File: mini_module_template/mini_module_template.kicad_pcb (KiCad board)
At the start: 4 copper layers, 100 x 50 mm, 135 parts, among them IC1 TJA1044GTK_3Z, J1 SWD, J4 USB_C_Receptacle_USB2.0, Q1 S9013, SW2 NRST, SW4 SW_DIP_x01, U1 STM32F303CBTx, U2 FM24CL16B, U3 STM32F103CB, U4 AZ1117-3.3, U5 TPS563200, U6 IP4220CZ6, U7 SL2.1A, Y1 8MHz, Y2 8MHz, Y4 12Mhz

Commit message: a
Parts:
- moved R35 0.42 mm to (165.2, 68.4)
- moved C33 0.39 mm to (165.4, 70.2)
- moved R33 0.16 mm to (164.0, 65.4)
- moved R34 0.16 mm to (164.0, 66.6)
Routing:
- net GND: track 95.7 -> 102.7 mm, vias 72 -> 76
- net /USB/USB_PROT_D+: track 6.66 -> 10.1 mm
- net +3V3: track 16.5 -> 19.4 mm, vias 32 -> 34
- net Net-(D1-A): track 25.4 -> 23.7 mm
- net /CAN/CANH: track 143.0 -> 144.6 mm
- net /MCU/USB_D-: track 41.1 -> 41.7 mm

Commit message: a
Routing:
- net /CAN/CANH: track 144.6 -> 109.2 mm
- net /CAN/CANL: track 146.0 -> 115.4 mm

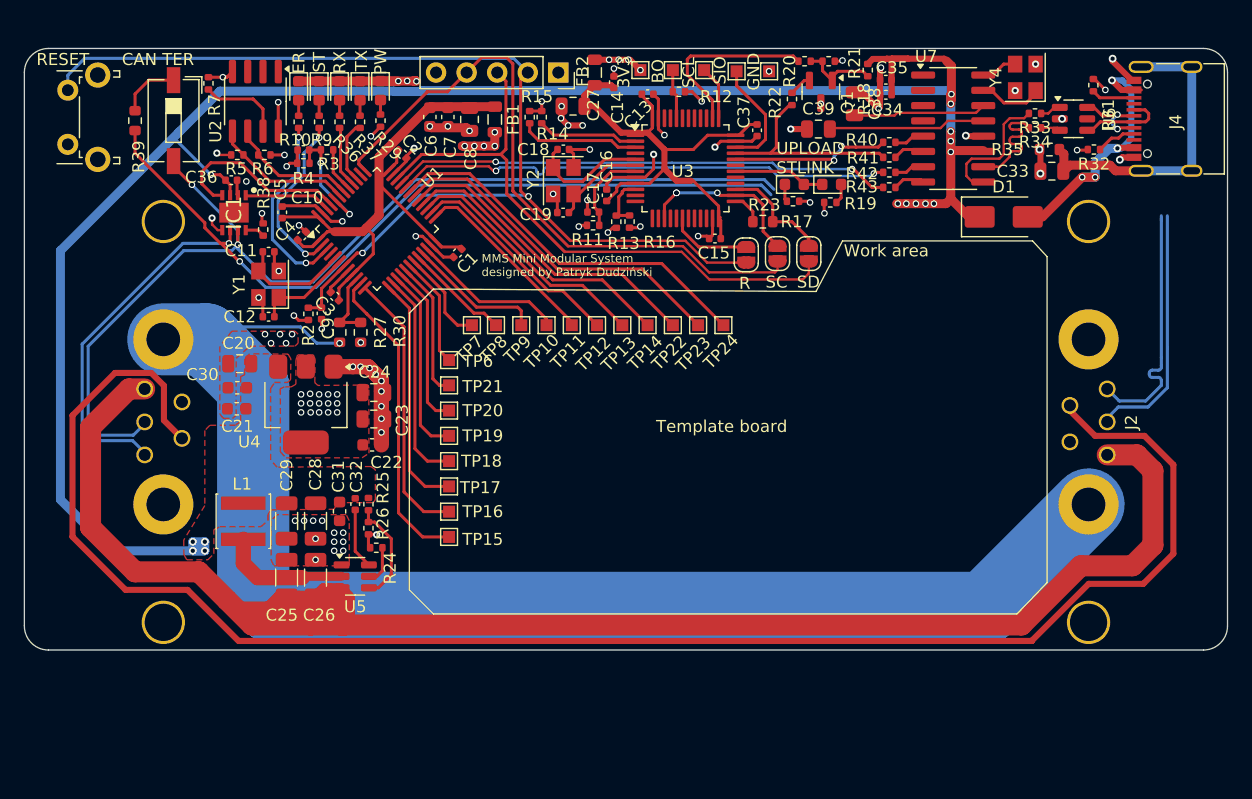
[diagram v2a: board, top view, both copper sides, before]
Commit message: fixed can and usb traces
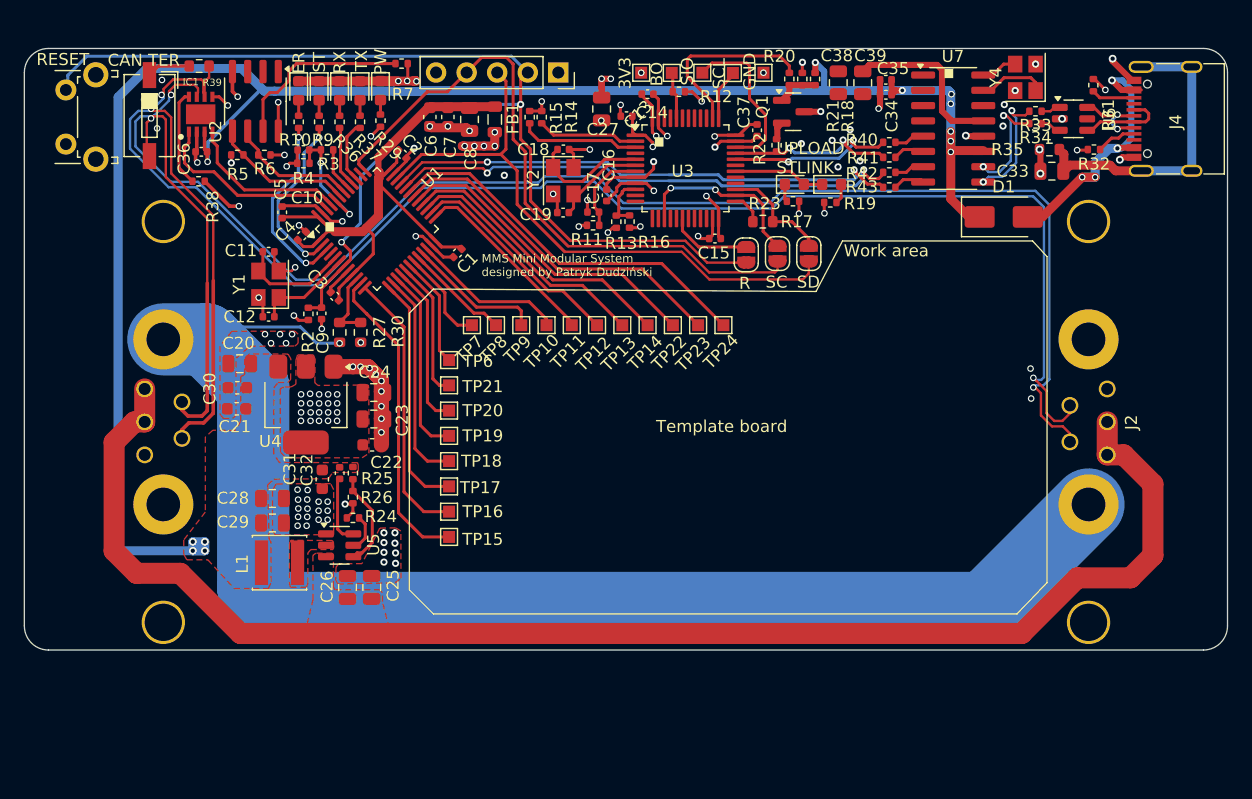
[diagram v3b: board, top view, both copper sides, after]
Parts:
- removed FB2: FerriteBead, Inductor_SMD:L_0805_2012Metric
- C25, C26, C28, C29: footprint Capacitor_SMD:C_1206_3216Metric -> Capacitor_SMD:C_0805_2012Metric
- moved R7 16.1 mm to (111.4, 61.3), turned to 180 degrees
- moved IC1 8.64 mm to (94.7, 65.5), turned to 90 degrees
- moved C25 7.11 mm to (108.9, 104.8)
- moved R39 7.00 mm to (94.5, 61.5), turned to 180 degrees
- moved R38 6.70 mm to (94.5, 71.0), turned to 180 degrees
- moved C39 5.33 mm to (149.7, 62.9), turned to 90 degrees
- moved L1 4.57 mm to (101.2, 102.7), turned to 180 degrees
- moved R18 4.44 mm to (145.7, 62.5)
- moved R22 4.06 mm to (142.5, 68.0)
- moved C28 4.04 mm to (100.6, 97.4), turned to 0 degrees
- moved C36 3.43 mm to (94.7, 68.6), turned to 180 degrees
- moved R24 3.15 mm to (107.3, 99.0)
- moved C31 3.03 mm to (104.8, 95.8)
- moved C14 3.02 mm to (130.1, 65.6), turned to 180 degrees
- moved C32 2.89 mm to (106.2, 95.3)
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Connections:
- net Net-(U5-SW) renamed /POWER/5V_COIL
- C13 pad 1: Net-(U3-VBAT) -> +3V3
- C14 pad 1: Net-(U3-VBAT) -> +3V3
- C15 pad 1: Net-(U3-VBAT) -> +3V3
- C16 pad 1: Net-(U3-VBAT) -> +3V3
- C27 pad 1: Net-(U3-VBAT) -> +3V3
- C37 pad 1: Net-(U3-VBAT) -> +3V3
- IC1 pad 6: /CAN/CANL -> /CAN/CAN-
- IC1 pad 7: /CAN/CANH -> /CAN/CAN+
- J2 pad 3: /CAN/CANH -> +12V
- J2 pad 4: /CAN/CANL -> GND
- J2 pad 5: GND -> /CAN/CAN+
- J2 pad 6: /POWER/NC -> /CAN/CAN-
- J3 pad 3: /CAN/CANH -> +12V
- J3 pad 4: /CAN/CANL -> GND
- J3 pad 5: GND -> /CAN/CAN+
- J3 pad 6: /POWER/NC -> /CAN/CAN-
- R39 pad 1: /CAN/CANL -> /CAN/CAN-
- SW4 pad 2: /CAN/CANH -> /CAN/CAN+
- U3 pad 1: Net-(U3-VBAT) -> +3V3
- U3 pad 24: Net-(U3-VBAT) -> +3V3
- U3 pad 36: Net-(U3-VBAT) -> +3V3
- U3 pad 48: Net-(U3-VBAT) -> +3V3
- U3 pad 9: Net-(U3-VBAT) -> +3V3
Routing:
- net /CAN/CAN-: track 0.00 -> 154.6 mm, vias 0 -> 3
- net /CAN/CAN+: track 0.00 -> 152.2 mm, vias 0 -> 3
- net /POWER/NC: track 141.0 -> 0.00 mm
- net /CAN/CANL: track 115.4 -> 0.00 mm, vias 2 -> 0
- net /CAN/CANH: track 109.2 -> 0.00 mm, vias 2 -> 0
- net Net-(U3-VBAT): track 40.2 -> 0.00 mm
- net +12V: track 150.7 -> 120.5 mm
- net +3V3: track 19.4 -> 36.3 mm, vias 34 -> 42
- net +5V: track 165.0 -> 153.1 mm, vias 15 -> 12
- net Net-(U7-VDD18): track 11.1 -> 0.00 mm
- net /POWER/5V_COIL: track 10.9 -> 0.00 mm
- net /CAN/CAN_TXD: track 7.17 -> 16.1 mm
- net Net-(U2-WP): track 6.75 -> 15.1 mm
- net /MCU/NRST: track 95.0 -> 101.7 mm
- net Net-(IC1-STB): track 1.64 -> 8.03 mm
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- added copper zone on F.Cu, net +12V
- added copper zone on F.Cu, net /POWER/5V_COIL
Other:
- board text added: "."

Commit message: rev 1.0 finished
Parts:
- added C40: 100n, Capacitor_SMD:C_0402_1005Metric, F.Cu at (157.3, 75.1)
- added C41: 1n, Capacitor_SMD:C_0402_1005Metric, F.Cu at (157.3, 73.2)
- added Q2: AO3400A, Package_TO_SOT_SMD:SOT-23, F.Cu at (97.0, 95.1)
- added R28: 1k, Resistor_SMD:R_0402_1005Metric, F.Cu at (96.2, 92.6)
- added R44: 100k, Resistor_SMD:R_0402_1005Metric, F.Cu at (96.0, 98.0)
- added R45: 10k, Resistor_SMD:R_0402_1005Metric, F.Cu at (158.7, 76.6)
- added R46: 22R, Resistor_SMD:R_0402_1005Metric, F.Cu at (152.0, 70.3)
- added R47: 22R, Resistor_SMD:R_0402_1005Metric, F.Cu at (151.9, 71.5)
- added U8: TS3USB30EDGSR, Package_SO:VSSOP-10_3x3mm_P0.5mm, F.Cu at (161.0, 74.3)
- added kibuzzard-673144D2: G***, kibuzzard-673144D2, B.Cu at (172.4, 91.1)
- added kibuzzard-673144DF: G***, kibuzzard-673144DF, B.Cu at (171.7, 93.8)
- added kibuzzard-673144EC: G***, kibuzzard-673144EC, B.Cu at (172.4, 88.3)
- added kibuzzard-6731459B: G***, kibuzzard-6731459B, B.Cu at (94.5, 91.0)
- added kibuzzard-673145AA: G***, kibuzzard-673145AA, B.Cu at (94.5, 93.9)
- added kibuzzard-673147F0: G***, kibuzzard-673147F0, F.Cu at (160.5, 92.5)
- added kibuzzard-673147F0: G***, kibuzzard-673147F0, B.Cu at (177.8, 90.5)
- added kibuzzard-67314807: G***, kibuzzard-67314807, B.Cu at (82.3, 91.1)
- added kibuzzard-67314D46: G***, kibuzzard-67314D46, F.Cu at (126.5, 78.7)
- added kibuzzard-6731503D: G***, kibuzzard-6731503D, B.Cu at (165.5, 88.3)
- added kibuzzard-67315047: G***, kibuzzard-67315047, B.Cu at (165.5, 91.3)
- added kibuzzard-673150A6: G***, kibuzzard-673150A6, B.Cu at (88.3, 88.3)
- added kibuzzard-673150B2: G***, kibuzzard-673150B2, B.Cu at (87.6, 91.0)
- added kibuzzard-673150BD: G***, kibuzzard-673150BD, B.Cu at (87.6, 93.8)
- added kibuzzard-673151BF: G***, kibuzzard-673151BF, F.Cu at (137.6, 92.3)
- C33: footprint Capacitor_SMD:C_0805_2012Metric -> Capacitor_SMD:C_0402_1005Metric
- C38, C39: footprint Capacitor_SMD:C_0805_2012Metric -> Capacitor_SMD:C_0603_1608Metric
- R35: footprint Resistor_SMD:R_0603_1608Metric -> Resistor_SMD:R_0402_1005Metric
- moved C38 16.8 mm to (163.5, 68.5)
- moved C39 13.4 mm to (161.9, 68.5)
- moved C30 11.5 mm to (106.2, 95.9), turned to -90 degrees
- moved R19 11.3 mm to (149.4, 61.7), turned to 90 degrees
- moved R23 10.2 mm to (149.0, 63.8), turned to -90 degrees
- moved D4 9.29 mm to (147.6, 62.0), turned to 90 degrees
- moved D1 9.14 mm to (152.3, 74.3)
- moved D5 7.22 mm to (147.6, 65.0), turned to 90 degrees
- moved R25 6.31 mm to (109.2, 101.3)
- moved R26 6.21 mm to (109.2, 103.2)
- moved C32 3.97 mm to (107.3, 99.1), turned to 0 degrees
- moved C25 3.19 mm to (106.0, 106.1), turned to 0 degrees
- moved R41 3.17 mm to (152.4, 65.9)
- moved R40 3.12 mm to (152.4, 64.7)
- moved R43 2.63 mm to (152.0, 68.9)
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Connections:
- C28 pad 1: +5V -> /POWER/5V_mosfet
- C29 pad 1: +5V -> /POWER/5V_mosfet
- C30 pad 1: +5V -> /POWER/5V_mosfet
- C31 pad 1: +5V -> /POWER/5V_mosfet
- C32 pad 1: +5V -> /POWER/5V_COIL
- D1 pad 2: Net-(D1-A) -> /USB/VBUS
- J2 pad 3: +12V -> /POWER/USB_UPSTREAM_D+
- J2 pad 4: GND -> /POWER/USB_UPSTREAM_D-
- J3 pad 3: +12V -> /POWER/USB_DOWNSTREAM_D+
- J3 pad 4: GND -> /POWER/USB_DOWNSTREAM_D-
- J4 pad A4: Net-(D1-A) -> /USB/VBUS
- J4 pad A9: Net-(D1-A) -> /USB/VBUS
- J4 pad B4: Net-(D1-A) -> /USB/VBUS
- J4 pad B9: Net-(D1-A) -> /USB/VBUS
- L1 pad 2: +5V -> /POWER/5V_mosfet
- R25 pad 1: +5V -> /POWER/5V_mosfet
- R33 pad 1: Net-(R33-Pad1) -> /USB/USB_CONN_D-
- R34 pad 1: Net-(R34-Pad1) -> /USB/USB_CONN_D+
- R40 pad 1: Net-(U7-DM2) -> Net-(U7-DM3)
- R41 pad 2: Net-(U7-DP2) -> Net-(U7-DP3)
- R42 pad 2: Net-(U7-DM1) -> Net-(U7-DM2)
- R43 pad 2: Net-(U7-DP1) -> Net-(U7-DP2)
- U6 pad 1: Net-(R33-Pad1) -> /USB/USB_CONN_D-
- U6 pad 3: Net-(R34-Pad1) -> /USB/USB_CONN_D+
- U6 pad 5: /USB/V_BUS -> /USB/VBUS
- U7 pad 10: /USB/USB_PROT_D+ -> /USB/USB_UPSTREAM_D+
- U7 pad 3: unconnected-(U7-DM3-Pad3) -> Net-(U7-DM3)
- U7 pad 4: unconnected-(U7-DP3-Pad4) -> Net-(U7-DP3)
- U7 pad 9: /USB/USB_PROT_D- -> /USB/USB_UPSTREAM_D-
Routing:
- net /POWER/USB_DOWNSTREAM_D-: track 0.00 -> 90.4 mm, vias 0 -> 1
- net /POWER/USB_DOWNSTREAM_D+: track 0.00 -> 89.0 mm, vias 0 -> 1
- net +12V: track 120.5 -> 178.7 mm
- net /USB/VBUS: track 0.00 -> 35.8 mm, vias 0 -> 2
- net /POWER/USB_UPSTREAM_D+: track 0.00 -> 28.0 mm, vias 0 -> 1
- net /POWER/USB_UPSTREAM_D-: track 0.00 -> 27.6 mm, vias 0 -> 1
- net /MCU/3V3_MCU: track 48.9 -> 21.8 mm
- net Net-(D1-A): track 23.7 -> 0.00 mm, vias 4 -> 0
- net VCC: track 116.8 -> 135.6 mm
- net GND: track 105.4 -> 119.4 mm, vias 97 -> 105
- net Net-(U7-VDD33): track 14.2 -> 3.25 mm
- net /POWER/5V_mosfet: track 0.00 -> 10.4 mm
- net /STLINK/LED: track 7.65 -> 14.1 mm
- net /USB/USB_UPSTREAM_D+: track 0.00 -> 6.41 mm
- net +3V3: track 36.3 -> 42.1 mm, vias 42 -> 43
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- added copper zone on F.Cu, net /MCU/3V3_MCU
- added copper zone on F.Cu, net /POWER/5V_mosfet
- added copper zone on F.Cu, net /USB/VBUS
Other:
- board size 100 x 50 mm -> 100 x 60 mm
- board text added: "MMS Mini Modular System designed by Patryk Dudziński REV1.0 11.11.2024"
- board text added: "QC"
- board text added: "S/N"
- board text added: "STLINK"
- board text removed: "12V"
- board text removed: "CANH"
- board text removed: "CANL"
- board text removed: "MMS Mini Modular System designed by Patryk Dudziński"
- board text removed: "NC"
- board text removed: "Template board"
- board text removed: "UPLOAD STLINK"
- board text removed: "VCC"
